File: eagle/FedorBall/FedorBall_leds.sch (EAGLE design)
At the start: 17 parts, among them U1 TLC5940-NT, U2 TLC5940-NT, U3 TLC5940-NT, U4 TLC5940-NT

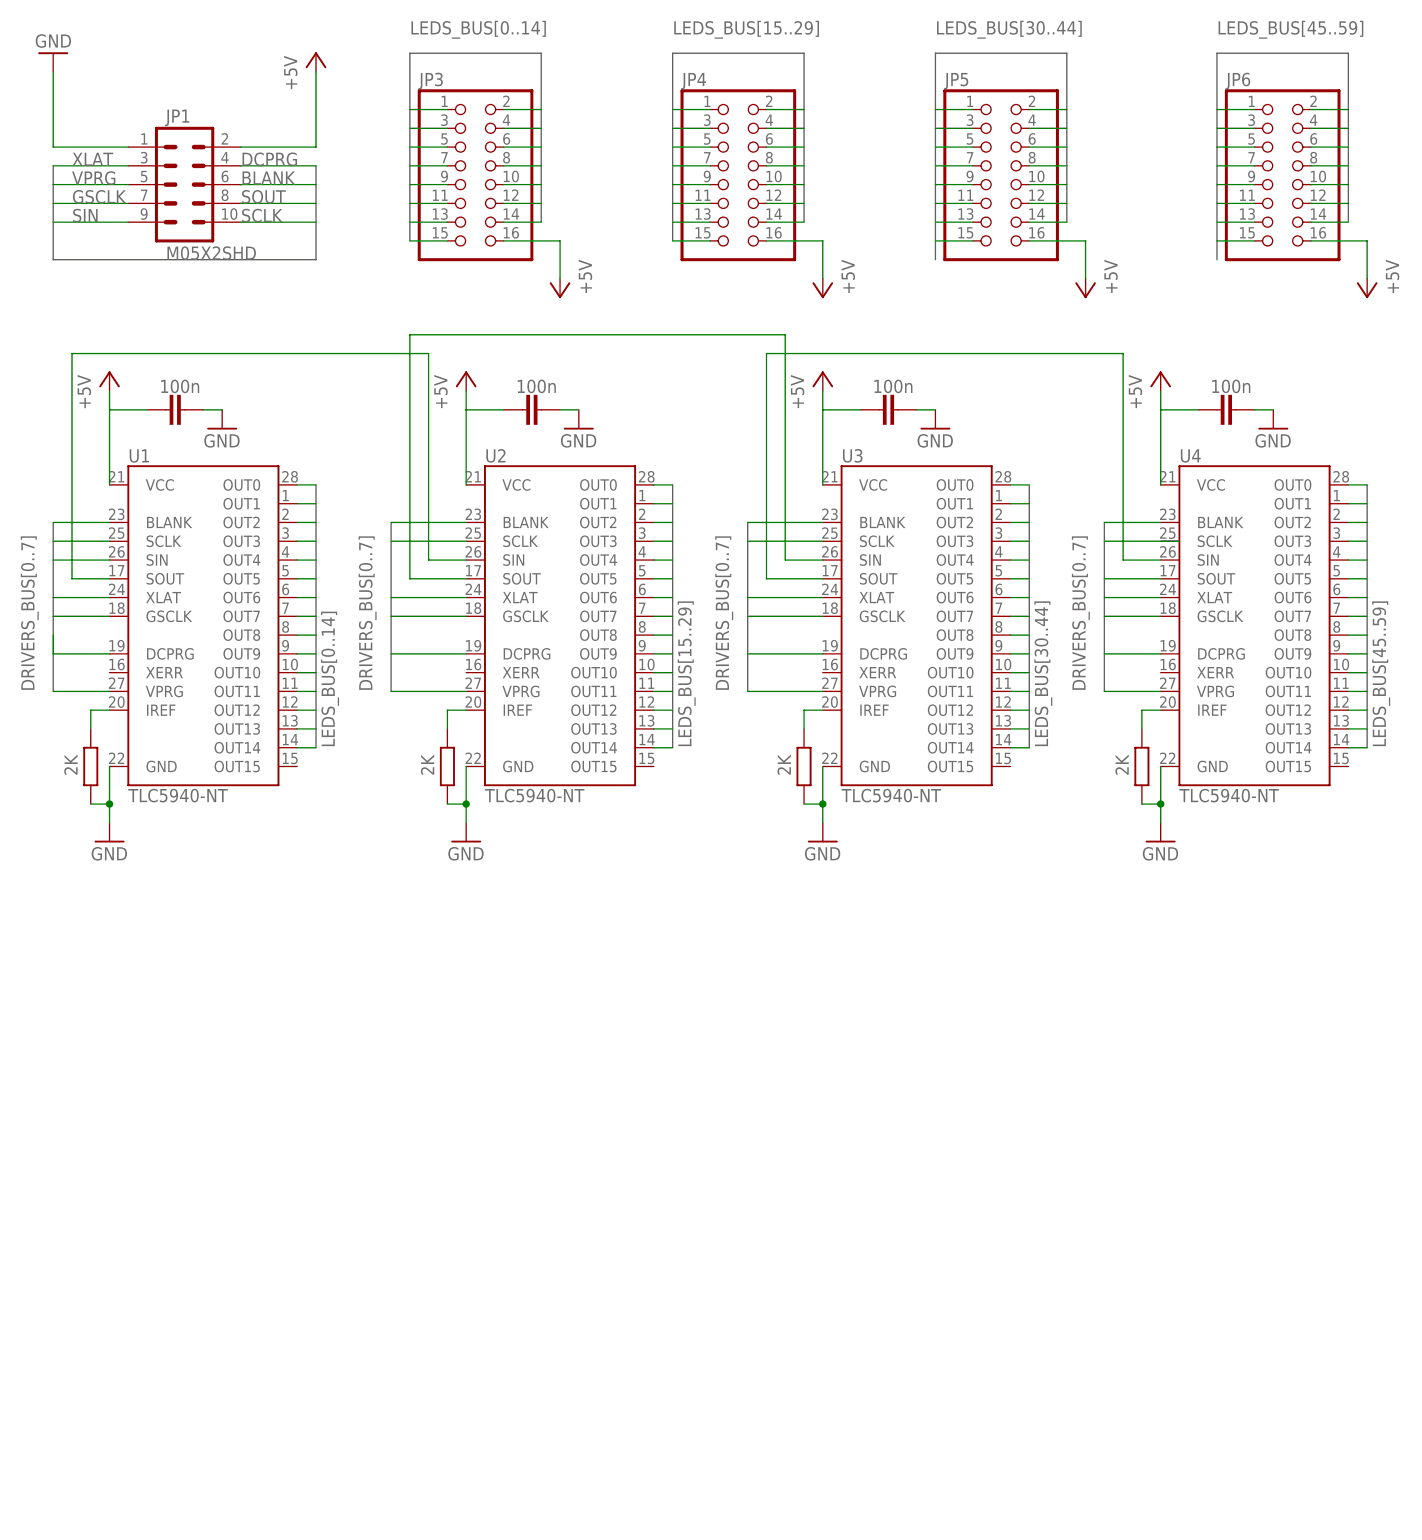
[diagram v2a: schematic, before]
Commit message: update leds board scheme
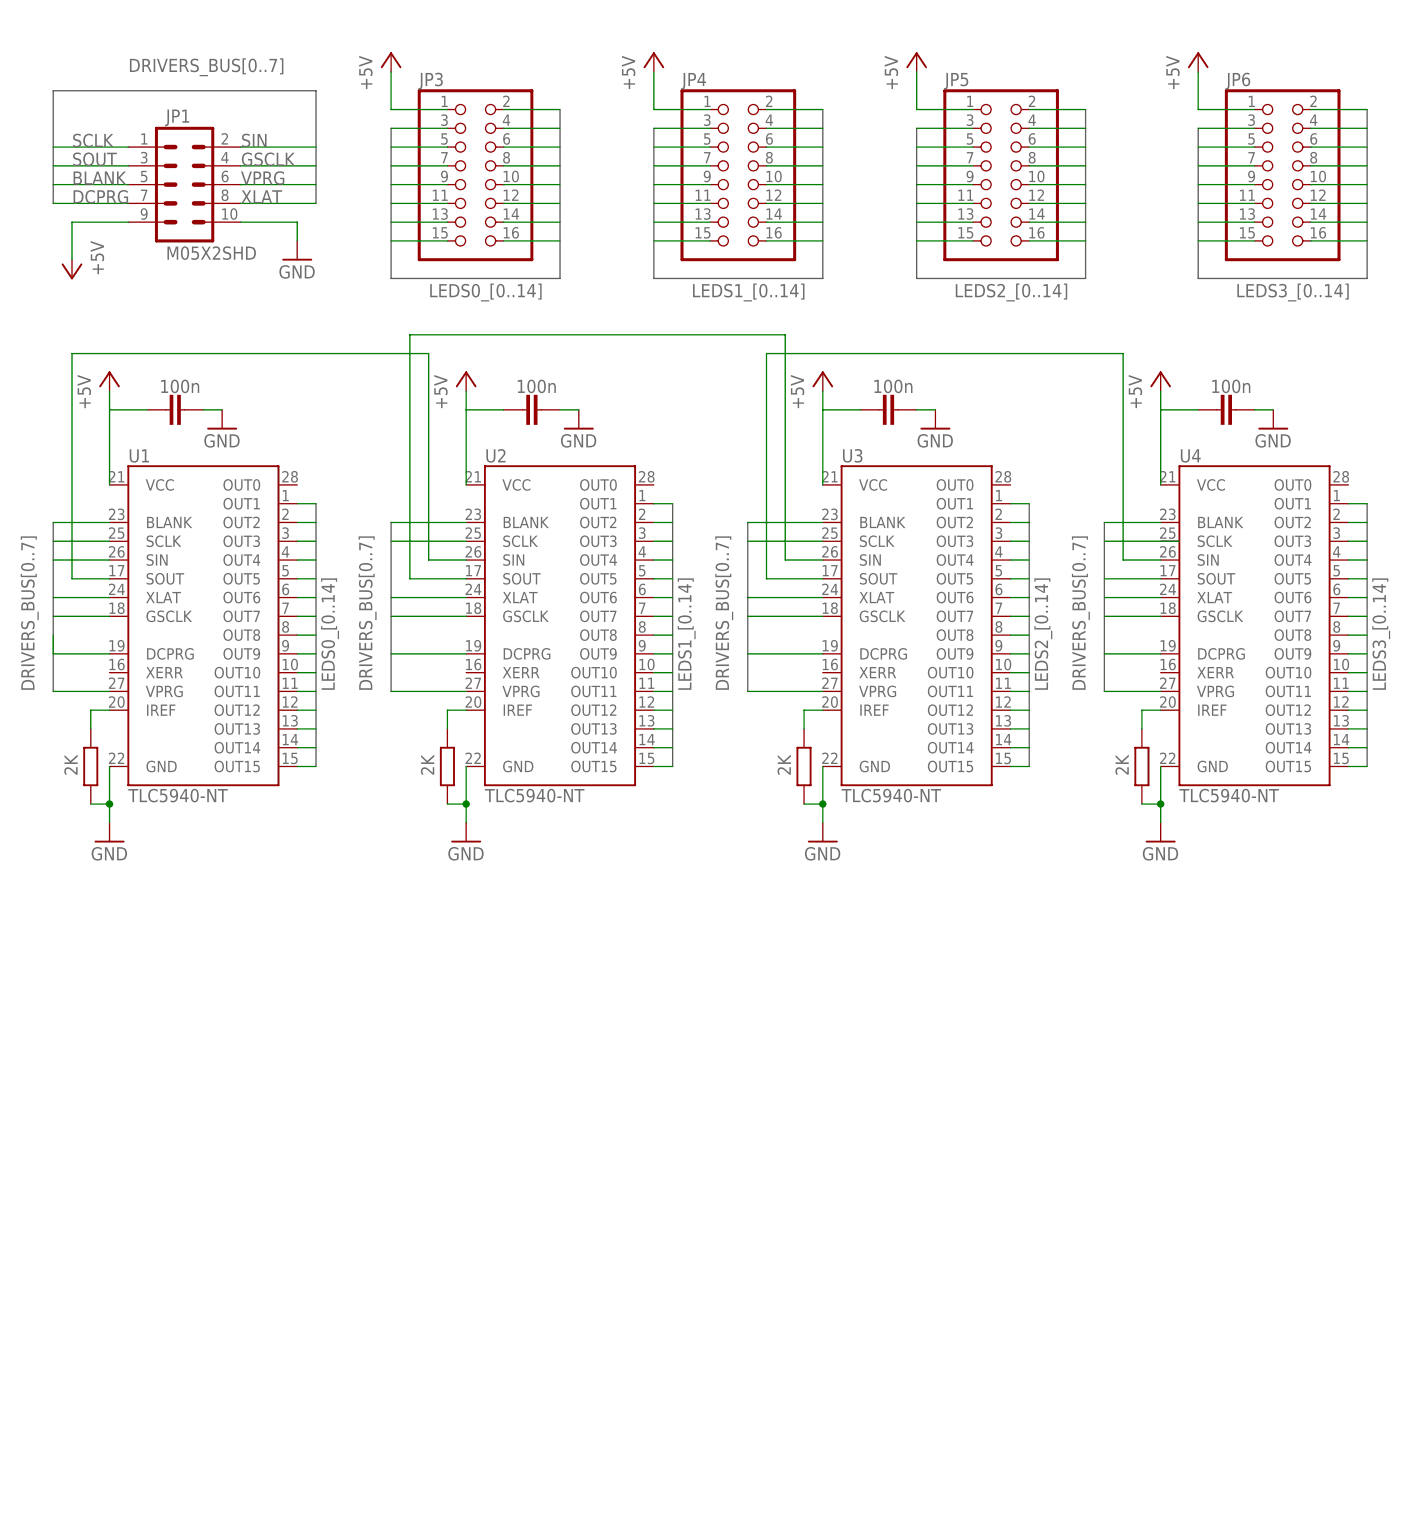
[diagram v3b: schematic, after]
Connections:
- removed net LEDS_BUS0: JP3.1, U1.OUT0
- removed net LEDS_BUS1: JP3.3, U1.OUT1
- removed net LEDS_BUS10: JP3.6, U1.OUT10
- removed net LEDS_BUS11: JP3.8, U1.OUT11
- removed net LEDS_BUS12: JP3.10, U1.OUT12
- removed net LEDS_BUS13: JP3.12, U1.OUT13
- removed net LEDS_BUS14: JP3.14, U1.OUT14
- removed net LEDS_BUS15: JP4.1, U2.OUT0
- removed net LEDS_BUS16: JP4.3, U2.OUT1
- removed net LEDS_BUS17: JP4.5, U2.OUT2
- removed net LEDS_BUS18: JP4.7, U2.OUT3
- removed net LEDS_BUS19: JP4.9, U2.OUT4
- removed net LEDS_BUS2: JP3.5, U1.OUT2
- removed net LEDS_BUS20: JP4.11, U2.OUT5
- removed net LEDS_BUS21: JP4.13, U2.OUT6
- removed net LEDS_BUS22: JP4.15, U2.OUT7
- removed net LEDS_BUS23: JP4.2, U2.OUT8
- removed net LEDS_BUS24: JP4.4, U2.OUT9
- removed net LEDS_BUS25: JP4.6, U2.OUT10
- removed net LEDS_BUS26: JP4.8, U2.OUT11
- removed net LEDS_BUS27: JP4.10, U2.OUT12
- removed net LEDS_BUS28: JP4.12, U2.OUT13
- removed net LEDS_BUS29: JP4.14, U2.OUT14
- removed net LEDS_BUS3: JP3.7, U1.OUT3
- removed net LEDS_BUS30: JP5.1, U3.OUT0
- removed net LEDS_BUS31: JP5.3, U3.OUT1
- removed net LEDS_BUS32: JP5.5, U3.OUT2
- removed net LEDS_BUS33: JP5.7, U3.OUT3
- removed net LEDS_BUS34: JP5.9, U3.OUT4
- removed net LEDS_BUS35: JP5.11, U3.OUT5
- removed net LEDS_BUS36: JP5.13, U3.OUT6
- removed net LEDS_BUS37: JP5.15, U3.OUT7
- removed net LEDS_BUS38: JP5.2, U3.OUT8
- removed net LEDS_BUS39: JP5.4, U3.OUT9
- removed net LEDS_BUS4: JP3.9, U1.OUT4
- removed net LEDS_BUS40: JP5.6, U3.OUT10
- removed net LEDS_BUS41: JP5.8, U3.OUT11
- removed net LEDS_BUS42: JP5.10, U3.OUT12
- removed net LEDS_BUS43: JP5.12, U3.OUT13
- removed net LEDS_BUS44: JP5.14, U3.OUT14
- removed net LEDS_BUS45: JP6.1, U4.OUT0
- removed net LEDS_BUS46: JP6.3, U4.OUT1
- removed net LEDS_BUS47: JP6.5, U4.OUT2
- removed net LEDS_BUS48: JP6.7, U4.OUT3
- removed net LEDS_BUS49: JP6.9, U4.OUT4
- removed net LEDS_BUS5: JP3.11, U1.OUT5
- removed net LEDS_BUS50: JP6.11, U4.OUT5
- removed net LEDS_BUS51: JP6.13, U4.OUT6
- removed net LEDS_BUS52: JP6.15, U4.OUT7
- removed net LEDS_BUS53: JP6.2, U4.OUT8
- removed net LEDS_BUS54: JP6.4, U4.OUT9
- removed net LEDS_BUS55: JP6.6, U4.OUT10
- removed net LEDS_BUS56: JP6.8, U4.OUT11
- removed net LEDS_BUS57: JP6.10, U4.OUT12
- removed net LEDS_BUS58: JP6.12, U4.OUT13
- removed net LEDS_BUS59: JP6.14, U4.OUT14
- removed net LEDS_BUS6: JP3.13, U1.OUT6
- removed net LEDS_BUS7: JP3.15, U1.OUT7
- removed net LEDS_BUS8: JP3.2, U1.OUT8
- removed net LEDS_BUS9: JP3.4, U1.OUT9
- new net LEDS0_0: JP3.16, U1.OUT1
- new net LEDS0_1: JP3.15, U1.OUT2
- new net LEDS0_10: JP3.6, U1.OUT11
- new net LEDS0_11: JP3.5, U1.OUT12
- new net LEDS0_12: JP3.4, U1.OUT13
- new net LEDS0_13: JP3.3, U1.OUT14
- new net LEDS0_14: JP3.2, U1.OUT15
- new net LEDS0_2: JP3.14, U1.OUT3
- new net LEDS0_3: JP3.13, U1.OUT4
- new net LEDS0_4: JP3.12, U1.OUT5
- new net LEDS0_5: JP3.11, U1.OUT6
- new net LEDS0_6: JP3.10, U1.OUT7
- new net LEDS0_7: JP3.9, U1.OUT8
- new net LEDS0_8: JP3.8, U1.OUT9
- new net LEDS0_9: JP3.7, U1.OUT10
- new net LEDS1_0: JP4.16, U2.OUT1
- new net LEDS1_1: JP4.15, U2.OUT2
- new net LEDS1_10: JP4.6, U2.OUT11
- new net LEDS1_11: JP4.5, U2.OUT12
- new net LEDS1_12: JP4.4, U2.OUT13
- new net LEDS1_13: JP4.3, U2.OUT14
- new net LEDS1_14: JP4.2, U2.OUT15
- new net LEDS1_2: JP4.14, U2.OUT3
- new net LEDS1_3: JP4.13, U2.OUT4
- new net LEDS1_4: JP4.12, U2.OUT5
- new net LEDS1_5: JP4.11, U2.OUT6
- new net LEDS1_6: JP4.10, U2.OUT7
- new net LEDS1_7: JP4.9, U2.OUT8
- new net LEDS1_8: JP4.8, U2.OUT9
- new net LEDS1_9: JP4.7, U2.OUT10
- new net LEDS2_0: JP5.16, U3.OUT1
- new net LEDS2_1: JP5.15, U3.OUT2
- new net LEDS2_10: JP5.6, U3.OUT11
- new net LEDS2_11: JP5.5, U3.OUT12
- new net LEDS2_12: JP5.4, U3.OUT13
- new net LEDS2_13: JP5.3, U3.OUT14
- new net LEDS2_14: JP5.2, U3.OUT15
- new net LEDS2_2: JP5.14, U3.OUT3
- new net LEDS2_3: JP5.13, U3.OUT4
- new net LEDS2_4: JP5.12, U3.OUT5
- new net LEDS2_5: JP5.11, U3.OUT6
- new net LEDS2_6: JP5.10, U3.OUT7
- new net LEDS2_7: JP5.9, U3.OUT8
- new net LEDS2_8: JP5.8, U3.OUT9
- new net LEDS2_9: JP5.7, U3.OUT10
- new net LEDS3_0: JP6.16, U4.OUT1
- new net LEDS3_1: JP6.15, U4.OUT2
- new net LEDS3_10: JP6.6, U4.OUT11
- new net LEDS3_11: JP6.5, U4.OUT12
- new net LEDS3_12: JP6.4, U4.OUT13
- new net LEDS3_13: JP6.3, U4.OUT14
- new net LEDS3_14: JP6.2, U4.OUT15
- new net LEDS3_2: JP6.14, U4.OUT3
- new net LEDS3_3: U4.OUT4
- new net LEDS3_4: JP6.12, U4.OUT5
- new net LEDS3_5: JP6.11, U4.OUT6
- new net LEDS3_6: JP6.10, U4.OUT7
- new net LEDS3_7: JP6.9, U4.OUT8
- new net LEDS3_8: JP6.8, U4.OUT9
- new net LEDS3_9: JP6.7, U4.OUT10
- net +5V: now also JP1.9, JP3.1, JP4.1, JP5.1, JP6.1; no longer JP1.2, JP3.16, JP4.16, JP5.16, JP6.16
- net DRIVERS_BUS0: now also JP1.5; no longer JP1.6
- net DRIVERS_BUS1: now also JP1.1; no longer JP1.10
- net DRIVERS_BUS2: now also JP1.2; no longer JP1.9
- net DRIVERS_BUS3: now also JP1.3; no longer JP1.8
- net DRIVERS_BUS4: now also JP1.8; no longer JP1.3
- net DRIVERS_BUS5: now also JP1.4; no longer JP1.7
- net DRIVERS_BUS6: now also JP1.7; no longer JP1.4
- net DRIVERS_BUS7: now also JP1.6; no longer JP1.5
- net GND: now also JP1.10; no longer JP1.1
